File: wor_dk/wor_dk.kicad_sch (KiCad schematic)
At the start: 8 parts

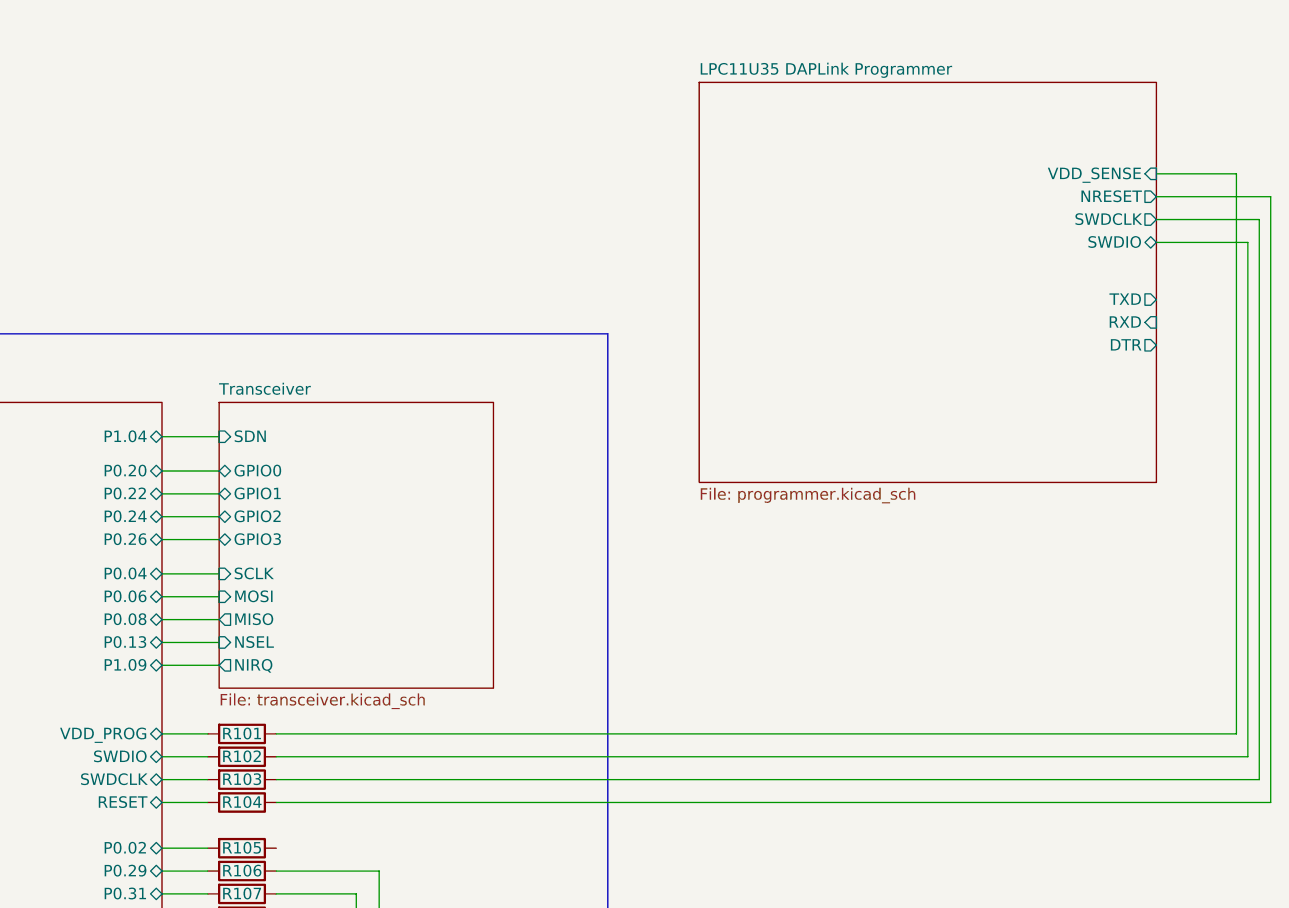
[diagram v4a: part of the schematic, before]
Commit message: wor_dk: remove VDD sense pin, add external SWD header
VDD sense is not useful since we do not support VDD level sensing and
the target voltage is always 3.3V.

The external SWD header allows using the board to program a third
party board (requires disconnecting the DUT first).
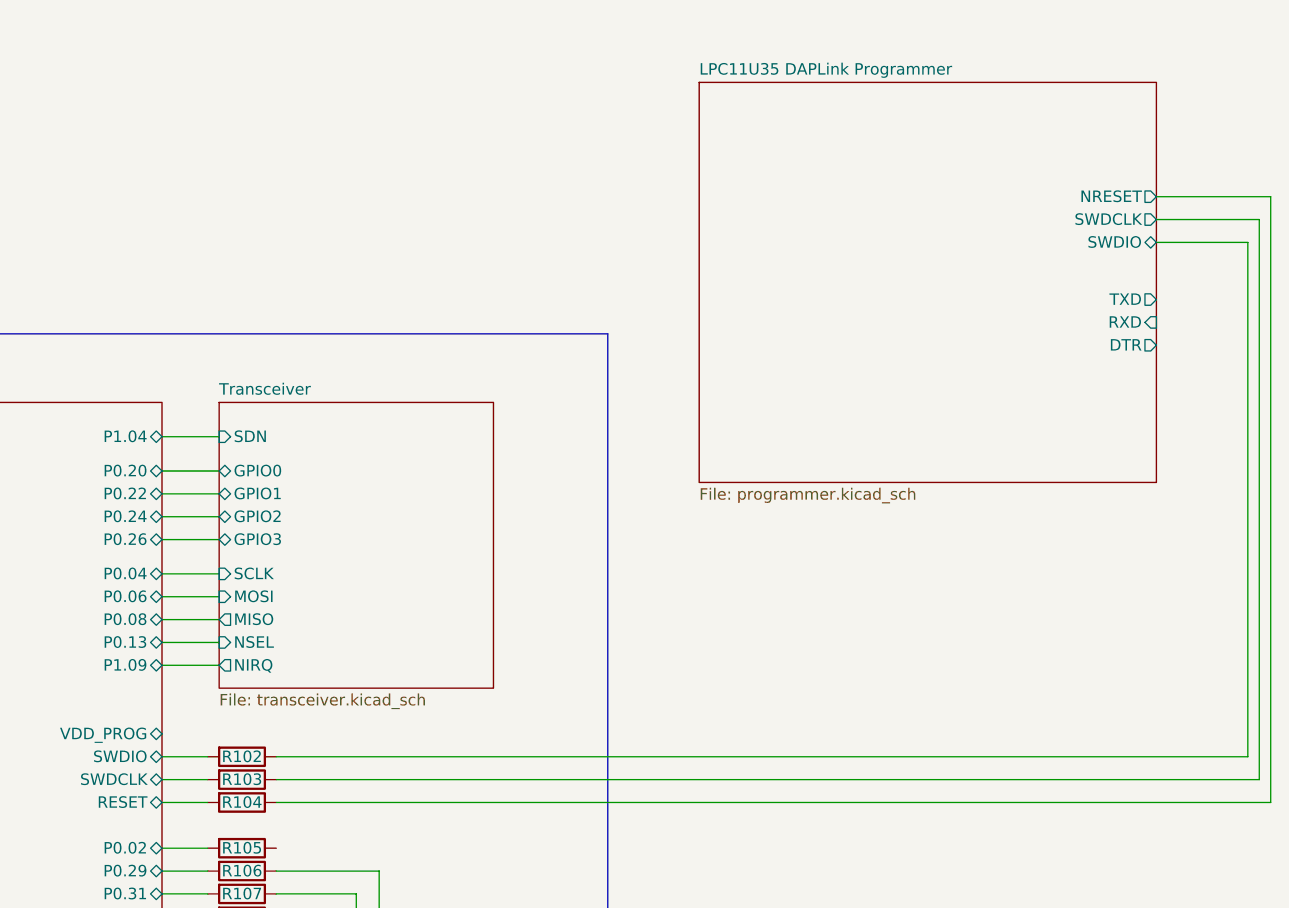
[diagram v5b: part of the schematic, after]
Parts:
- removed R101: 0, symbol Device:R
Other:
- sheet LPC11U35 DAPLink Programmer ports: added none; removed VDD_SENSE
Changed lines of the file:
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@@
-	(wire
-		(pts
-			(xy 140.97 100.33) (xy 146.05 100.33)
-		)
-		(stroke
-			(width 0)
-			(type default)
-		)
-	)
-	(wire
-		(pts
-			(xy 153.67 100.33) (xy 260.35 100.33)
-		)
-		(stroke
-			(width 0)
-			(type default)
-		)
-	)
 	(wire
 		(pts
@@
 	(wire
 		(pts
-			(xy 260.35 100.33) (xy 260.35 38.1)
-		)
-		(stroke
-			(width 0)
-			(type default)
-		)
-	)
-	(wire
-		(pts
 			(xy 140.97 105.41) (xy 146.05 105.41)
 		)
@@
 		(pts
 			(xy 93.98 102.87) (xy 99.06 102.87)
-		)
-		(stroke
-			(width 0)
-			(type default)
-		)
-	)
-	(wire
-		(pts
-			(xy 260.35 38.1) (xy 251.46 38.1)
 		)
 		(stroke
@@
 	(symbol
 		(lib_id "Device:R")
-		(at 149.86 100.33 270)
-		(unit 1)
-		(exclude_from_sim no)
-		(in_bom yes)
-		(on_board yes)
-		(dnp no)
-		(property "Reference" "R101"
-			(at 149.86 100.33 90)
-			(effects
-				(font
-					(size 1.27 1.27)
-				)
-			)
-		)
-		(property "Value" "0"
-			(at 149.86 102.362 90)
-			(effects
-				(font
-					(size 1.27 1.27)
-				)
-				(hide yes)
-			)
-		)
-		(property "Footprint" ""
-			(at 149.86 98.552 90)
-			(effects
-				(font
-					(size 1.27 1.27)
-				)
-				(hide yes)
-			)
-		)
-		(property "Datasheet" "~"
-			(at 149.86 100.33 0)
-			(effects
-				(font
-					(size 1.27 1.27)
-				)
-				(hide yes)
-			)
-		)
-		(property "Description" "Resistor"
-			(at 149.86 100.33 0)
-			(effects
-				(font
-					(size 1.27 1.27)
-				)
-				(hide yes)
-			)
-		)
-		(pin "1"
-		)
-		(pin "2"
-		)
-		(instances
-			(project ""
-				(path "/8d3147eb-060b-4f65-bf42-ed06a58b21ba"
-					(reference "R101")
-					(unit 1)
-				)
-			)
-		)
-	)
-	(symbol
-		(lib_id "Device:R")
 		(at 149.86 113.03 270)
 		(unit 1)
@@
 			(effects
 				(font
-					(size 1.27 1.27)
-				)
-				(justify right)
-			)
-		)
-		(pin "VDD_SENSE" input
-			(at 251.46 38.1 0)
-			(effects
-				(font

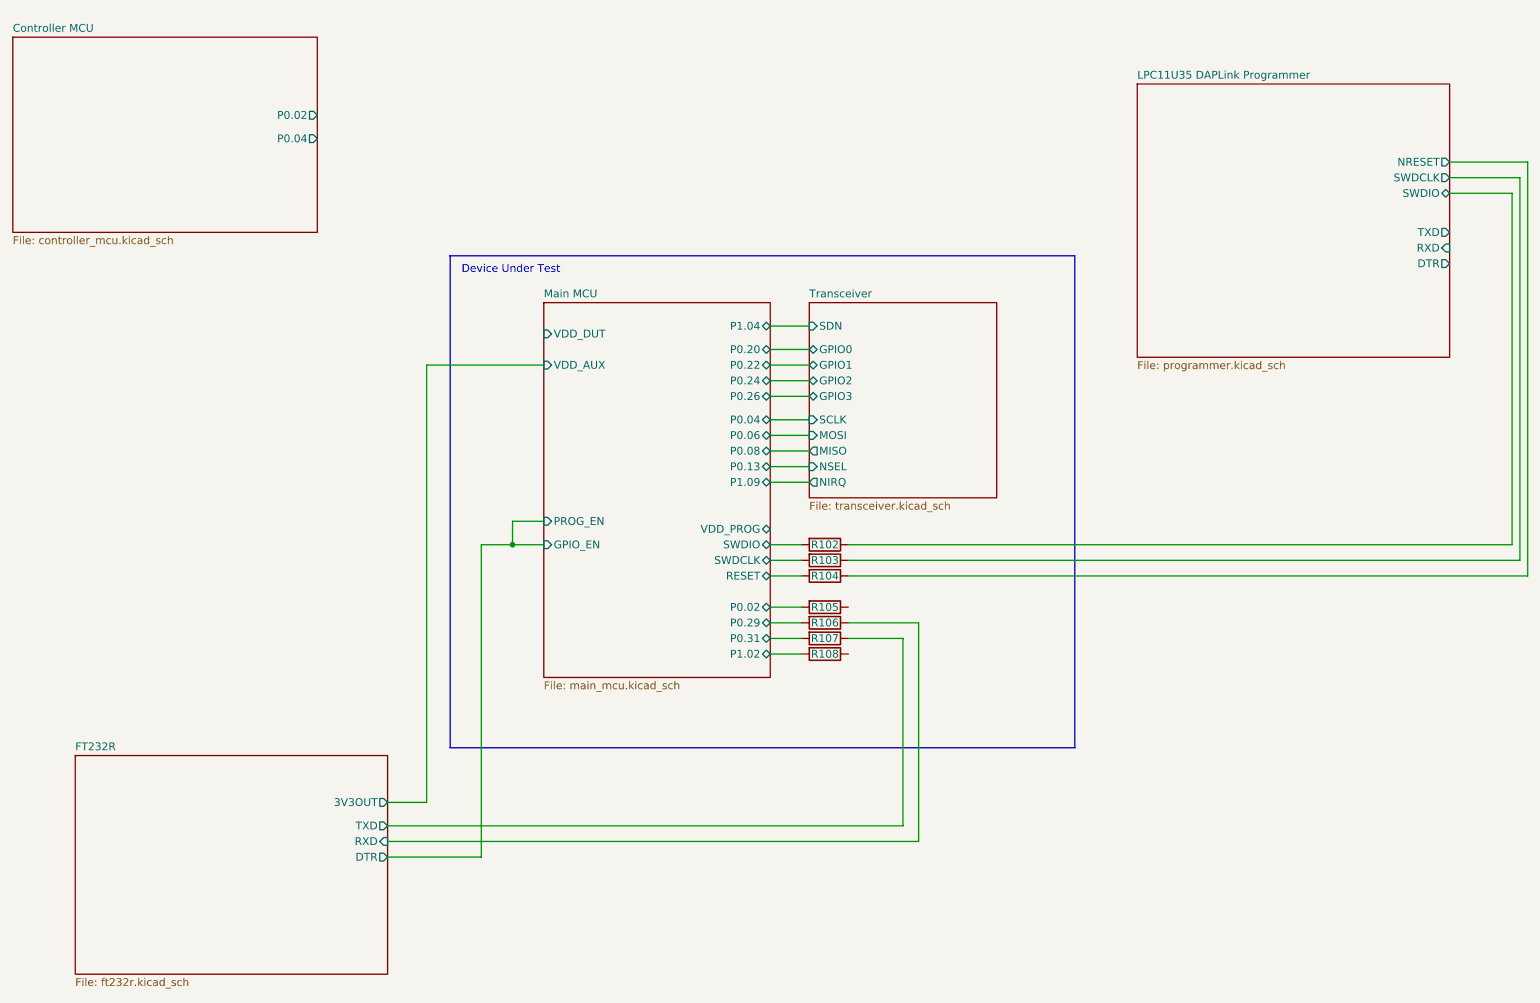
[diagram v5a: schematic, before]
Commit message: wor_dk: remove controller & re-annotate schematics
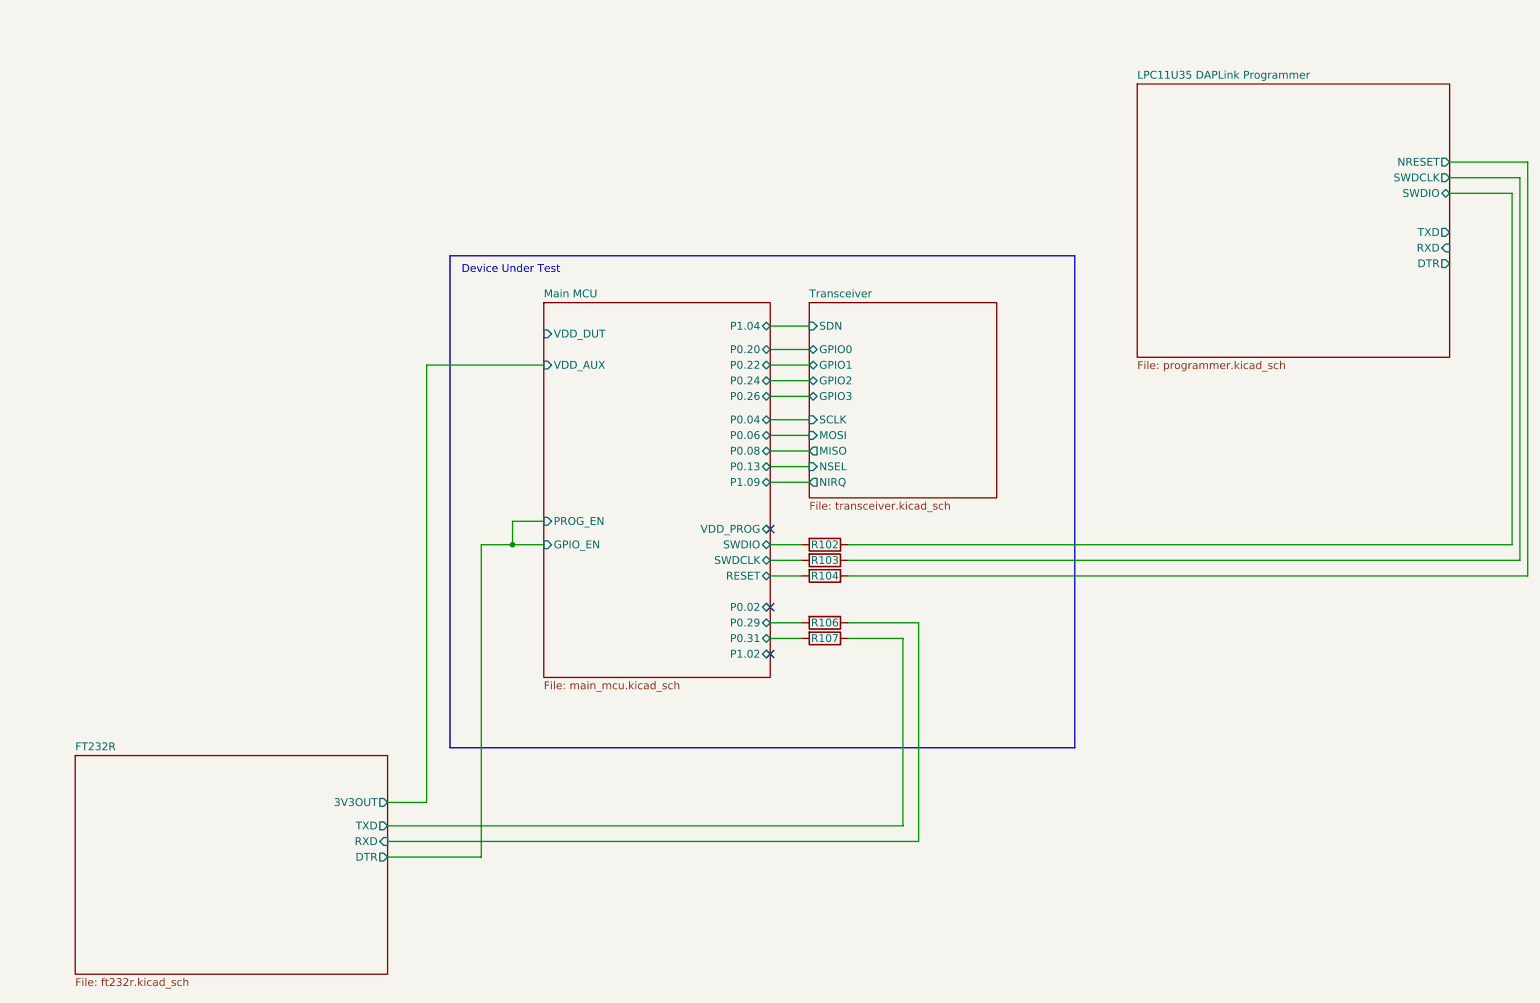
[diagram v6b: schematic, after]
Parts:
- removed R105, R108: 0, symbol Device:R
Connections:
- no-connect marks 0 -> 3
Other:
- removed sheet Controller MCU
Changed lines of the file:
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@@
 		(color 0 0 0 0)
 	)
+	(no_connect
+		(at 140.97 113.03)
+	)
+	(no_connect
+		(at 140.97 100.33)
+	)
+	(no_connect
+		(at 140.97 120.65)
+	)
 	(wire
 		(pts
@@
 	(wire
 		(pts
-			(xy 140.97 113.03) (xy 146.05 113.03)
-		)
-		(stroke
-			(width 0)
-			(type default)
-		)
-	)
-	(wire
-		(pts
 			(xy 162.56 148.59) (xy 162.56 118.11)
 		)
@@
 		(pts
 			(xy 251.46 43.18) (xy 262.89 43.18)
-		)
-		(stroke
-			(width 0)
-			(type default)
-		)
-	)
-	(wire
-		(pts
-			(xy 140.97 120.65) (xy 146.05 120.65)
 		)
 		(stroke
@@
 	(symbol
 		(lib_id "Device:R")
-		(at 149.86 120.65 270)
-		(unit 1)
-		(exclude_from_sim no)
-		(in_bom yes)
-		(on_board yes)
-		(dnp no)
-		(property "Reference" "R108"
-			(at 149.86 120.65 90)
-			(effects
-				(font
-					(size 1.27 1.27)
-				)
-			)
-		)
-		(property "Value" "0"
-			(at 149.86 122.682 90)
-			(effects
-				(font
-					(size 1.27 1.27)
-				)
-				(hide yes)
-			)
-		)
-		(property "Footprint" ""
-			(at 149.86 118.872 90)
-			(effects
-				(font
-					(size 1.27 1.27)
-				)
-				(hide yes)
-			)
-		)
-		(property "Datasheet" "~"
-			(at 149.86 120.65 0)
-			(effects
-				(font
-					(size 1.27 1.27)
-				)
-				(hide yes)
-			)
-		)
-		(property "Description" "Resistor"
-			(at 149.86 120.65 0)
-			(effects
-				(font
-					(size 1.27 1.27)
-				)
-				(hide yes)
-			)
-		)
-		(pin "1"
-		)
-		(pin "2"
-		)
-		(instances
-			(project "wor_dk"
-				(path "/8d3147eb-060b-4f65-bf42-ed06a58b21ba"
-					(reference "R108")
-					(unit 1)
-				)
-			)
-		)
-	)
-	(symbol
-		(lib_id "Device:R")
 		(at 149.86 105.41 270)
 		(unit 1)
@@
 				(path "/8d3147eb-060b-4f65-bf42-ed06a58b21ba"
 					(reference "R103")
-					(unit 1)
-				)
-			)
-		)
-	)
-	(symbol
-		(lib_id "Device:R")
-		(at 149.86 113.03 270)
-		(unit 1)
-		(exclude_from_sim no)
-		(in_bom yes)
-		(on_board yes)
-		(dnp no)
-		(property "Reference" "R105"
-			(at 149.86 113.03 90)
-			(effects
-				(font
-					(size 1.27 1.27)
-				)
-			)
-		)
-		(property "Value" "0"
-			(at 149.86 115.062 90)
-			(effects
-				(font
-					(size 1.27 1.27)
-				)
-				(hide yes)
-			)
-		)
-		(property "Footprint" ""
-			(at 149.86 111.252 90)
-			(effects
-				(font
-					(size 1.27 1.27)
-				)
-				(hide yes)
-			)
-		)
-		(property "Datasheet" "~"
-			(at 149.86 113.03 0)
-			(effects
-				(font
-					(size 1.27 1.27)
-				)
-				(hide yes)
-			)
-		)
-		(property "Description" "Resistor"
-			(at 149.86 113.03 0)
-			(effects
-				(font
-					(size 1.27 1.27)
-				)
-				(hide yes)
-			)
-		)
-		(pin "1"
-		)
-		(pin "2"
-		)
-		(instances
-			(project "wor_dk"
-				(path "/8d3147eb-060b-4f65-bf42-ed06a58b21ba"
-					(reference "R105")
 					(unit 1)
 				)
@@
 	)
 	(sheet
-		(at 17.78 20.32)
-		(size 49.53 31.75)
+		(at 27.94 137.16)
+		(size 50.8 35.56)
 		(fields_autoplaced yes)
 		(stroke
@@
 			(color 0 0 0 0.0000)
 		)
-		(property "Sheetname" "Controller MCU"
-			(at 17.78 19.6084 0)
+		(property "Sheetname" "FT232R"
+			(at 27.94 136.4484 0)
 			(effects
 				(font
@@
 			)
 		)
-		(property "Sheetfile" "controller_mcu.kicad_sch"
-			(at 17.78 52.6546 0)
+		(property "Sheetfile" "ft232r.kicad_sch"
+			(at 27.94 173.3046 0)
 			(effects
 				(font
@@
 			)
 		)
-		(pin "P0.02" output
-			(at 67.31 33.02 0)
+		(pin "3V3OUT" output
+			(at 78.74 144.78 0)
 			(effects
 				(font
@@
 			)
 		)
-		(pin "P0.04" output
-			(at 67.31 36.83 0)
+		(pin "TXD" output
+			(at 78.74 148.59 0)
+			(effects
+				(font
+					(size 1.27 1.27)
+				)
+				(justify right)
+			)
+		)
+		(pin "RXD" input
+			(at 78.74 151.13 0)
+			(effects
+				(font
+					(size 1.27 1.27)
+				)
+				(justify right)
+			)
+		)
+		(pin "DTR" output
+			(at 78.74 153.67 0)
 			(effects
 				(font
@@
 	)
 	(sheet
-		(at 27.94 137.16)
-		(size 50.8 35.56)
+		(at 200.66 27.94)
+		(size 50.8 44.45)
 		(fields_autoplaced yes)
 		(stroke
@@
 			(color 0 0 0 0.0000)
 		)
-		(property "Sheetname" "FT232R"
-			(at 27.94 136.4484 0)
+		(property "Sheetname" "LPC11U35 DAPLink Programmer"
+			(at 200.66 27.2284 0)
 			(effects
 				(font
@@
 			)
 		)
-		(property "Sheetfile" "ft232r.kicad_sch"
-			(at 27.94 173.3046 0)
+		(property "Sheetfile" "programmer.kicad_sch"
+			(at 200.66 72.9746 0)
 			(effects
 				(font
@@
 			)
 		)
-		(pin "3V3OUT" output
-			(at 78.74 144.78 0)
+		(pin "NRESET" output
+			(at 251.46 40.64 0)
 			(effects
 				(font
@@
 			)
 		)
+		(pin "DTR" output
+			(at 251.46 57.15 0)
+			(effects
+				(font
+					(size 1.27 1.27)
+				)
+				(justify right)
+			)
+		)
+		(pin "SWDCLK" output
+			(at 251.46 43.18 0)
+			(effects
+				(font
+					(size 1.27 1.27)
+				)
+				(justify right)
+			)
+		)
+		(pin "SWDIO" bidirectional
+			(at 251.46 45.72 0)
+			(effects
+				(font
+					(size 1.27 1.27)
+				)
+				(justify right)
+			)
+		)
 		(pin "TXD" output
-			(at 78.74 148.59 0)
+			(at 251.46 52.07 0)
 			(effects
 				(font
@@
 		)
 		(pin "RXD" input
-			(at 78.74 151.13 0)
-			(effects
-				(font
-					(size 1.27 1.27)
-				)
-				(justify right)
-			)
-		)
-		(pin "DTR" output
-			(at 78.74 153.67 0)
+			(at 251.46 54.61 0)
 			(effects
 				(font
@@
 				)
 			)
-		)
-	)
-	(sheet
-		(at 200.66 27.94)
-		(size 50.8 44.45)
-		(fields_autoplaced yes)
-		(stroke
-			(width 0.1524)
-			(type solid)
-		)
-		(fill
-			(color 0 0 0 0.0000)
-		)
-		(property "Sheetname" "LPC11U35 DAPLink Programmer"
-			(at 200.66 27.2284 0)
-			(effects
-				(font
-					(size 1.27 1.27)
-				)
-				(justify left bottom)
-			)
-		)
-		(property "Sheetfile" "programmer.kicad_sch"
-			(at 200.66 72.9746 0)
-			(effects
-				(font
-					(size 1.27 1.27)
-				)
-				(justify left top)
-			)
-		)
-		(pin "NRESET" output
-			(at 251.46 40.64 0)
-			(effects
-				(font
-					(size 1.27 1.27)
-				)
-				(justify right)
-			)
-		)
-		(pin "DTR" output
-			(at 251.46 57.15 0)
-			(effects
-				(font
-					(size 1.27 1.27)
-				)
-				(justify right)
-			)
-		)
-		(pin "SWDCLK" output
-			(at 251.46 43.18 0)
-			(effects
-				(font
-					(size 1.27 1.27)
-				)
-				(justify right)
-			)
-		)
-		(pin "SWDIO" bidirectional
-			(at 251.46 45.72 0)
-			(effects
-				(font
-					(size 1.27 1.27)
-				)
-				(justify right)
-			)
-		)
-		(pin "TXD" output
-			(at 251.46 52.07 0)
-			(effects
-				(font
-					(size 1.27 1.27)
-				)
-				(justify right)
-			)
-		)
-		(pin "RXD" input
-			(at 251.46 54.61 0)
-			(effects
-				(font
-					(size 1.27 1.27)
-				)
-				(justify right)
-			)
-		)
-		(instances
-			(project "wor_dk"
-				(path "/8d3147eb-060b-4f65-bf42-ed06a58b21ba"
-					(page "6")
-				)
-			)
